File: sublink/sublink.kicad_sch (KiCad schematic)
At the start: 27 parts

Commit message: wip schematic probably done
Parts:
- removed BT?: L402036, symbol Device:Battery
- removed C?: 100n, symbol Device:C
- removed D? (x15): LED, symbol Device:LED
- removed Q? (x4): Q_NMOS_DGS, symbol Device:Q_NMOS_DGS
- removed Q?: Q_PMOS_DGS, symbol Device:Q_PMOS_DGS
- removed R?: 330, symbol Device:R
- removed R?: 2k7, symbol Device:R
- removed U?: ATtiny414-SS, Package_SO:SOIC-14_3.9x8.7mm_P1.27mm, symbol MCU_Microchip_ATtiny:ATtiny414-SS
- removed U?: 4001, symbol 4xxx:4001
- removed U?: AP9101CK, Package_TO_SOT_SMD:SOT-23-5, symbol Battery_Management:AP9101CK
- added BT1: 3V7, Connector_PinHeader_2.54mm:PinHeader_1x02_P2.54mm_Vertical, symbol Device:Battery
- added D1, D2, D3: LED, LED_SMD:LED_0805_2012Metric_Pad1.15x1.40mm_HandSolder, symbol Device:LED
- added D10, D11, D12, D13, D14, D15, D16, D17, D18, D19, D20, D21, D4, D5, D6, D7, D8, D9: LED_Small, LED_SMD:LED_0805_2012Metric_Pad1.15x1.40mm_HandSolder, symbol Device:LED_Small
- added D22: DNP, Diode_SMD:D_SOD-323_HandSoldering, symbol Device:D_Small
- added D23: BAS21HT1G, Diode_SMD:D_SOD-323_HandSoldering, symbol Device:D_Small
- added J1: Conn_01x03_Female, Connector_PinHeader_2.54mm:PinHeader_1x03_P2.54mm_Horizontal, symbol Connector:Conn_01x03_Female
- added Q1: YJL2305A, Package_TO_SOT_SMD:SOT-23, symbol Device:Q_PMOS_DGS
- added R1, R2, R3, R4, R5, R6, R7, R8: R_Small, Resistor_SMD:R_0805_2012Metric_Pad1.20x1.40mm_HandSolder, symbol Device:R_Small
- added R9: 10k, Resistor_SMD:R_0805_2012Metric_Pad1.20x1.40mm_HandSolder, symbol Device:R_Small
- added SW1, SW2, SW3: SW_Push, Button_Switch_SMD:SW_SPST_Omron_B3FS-100xP, symbol Switch:SW_Push
- added U1: ATtiny414-SS, Package_SO:SOIC-14_3.9x8.7mm_P1.27mm, symbol MCU_Microchip_ATtiny:ATtiny414-SS
- added U2: OKY3402, sublink_custom:OKY3402, symbol custom_sublink:OKY3402
- added U3: JS202011, sublink_custom:JS202011, symbol custom_sublink:JS202011
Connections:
- net GND: now also BT1.2 (-), D1.1 (K), D2.1 (K), D3.1 (K), J1.1 (Pin_1), R9.1, SW1.1, SW2.1, SW3.1, U1.14 (GND), U2.1 (USB-), U2.3 (B-)
- net UPDI: now also J1.2 (Pin_2), U1.10 (~{RESET}/PA0)
- new net: D23.2 (A), Q1.2 (G), R9.2, U2.2 (USB+)
- new net: BT1.1 (+), D22.2 (A), Q1.1 (D), U2.4 (B+)
- new net: R4.2, U1.13 (PA3)
- new net: J1.3 (Pin_3), U3.3
- new net: D2.2 (A), R2.2
- new net: R6.2, U1.3 (PA5)
- new net: R2.1, U1.8 (PB1)
- new net: R1.1, U1.9 (PB0)
- new net: D1.2 (A), R1.2
- new net: R7.2, U1.4 (PA6)
- new net: D3.2 (A), R3.2
- new net: D22.1 (K), D23.1 (K), Q1.3 (S), U3.1
- new net: R3.1, U1.7 (PB2)
- new net: R5.2, U1.2 (PA4)
- new net: R8.2, U1.5 (PA7)
- new net L0: D4.2 (A), D5.1 (K), D6.1 (K), D7.2 (A), D8.1 (K), D9.2 (A), R4.1
- new net L1: D10.1 (K), D11.2 (A), D12.1 (K), D13.2 (A), D20.1 (K), D21.2 (A), D6.2 (A), D7.1 (K), R5.1
- new net L2: D10.2 (A), D11.1 (K), D14.1 (K), D15.2 (A), D18.1 (K), D19.2 (A), D8.2 (A), D9.1 (K), R6.1
- new net L3: D12.2 (A), D13.1 (K), D14.2 (A), D15.1 (K), D16.1 (K), D17.2 (A), D4.1 (K), D5.2 (A), R7.1
- new net L4: D16.2 (A), D17.1 (K), D18.2 (A), D19.1 (K), D20.2 (A), D21.1 (K), R8.1
- new net VCC: U1.1 (VCC), U3.5
- new net butt1: SW1.2, U1.6 (PB3)
- new net butt2: SW2.2, U1.11 (PA1)
- new net butt3: SW3.2, U1.12 (PA2)
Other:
- note added: "Pullups internal"

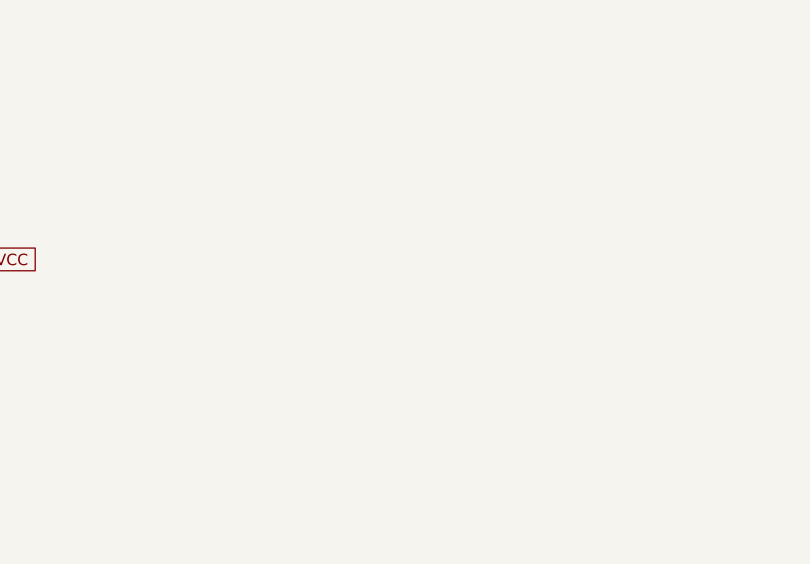
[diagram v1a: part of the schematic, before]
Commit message: wip board outline, led placement
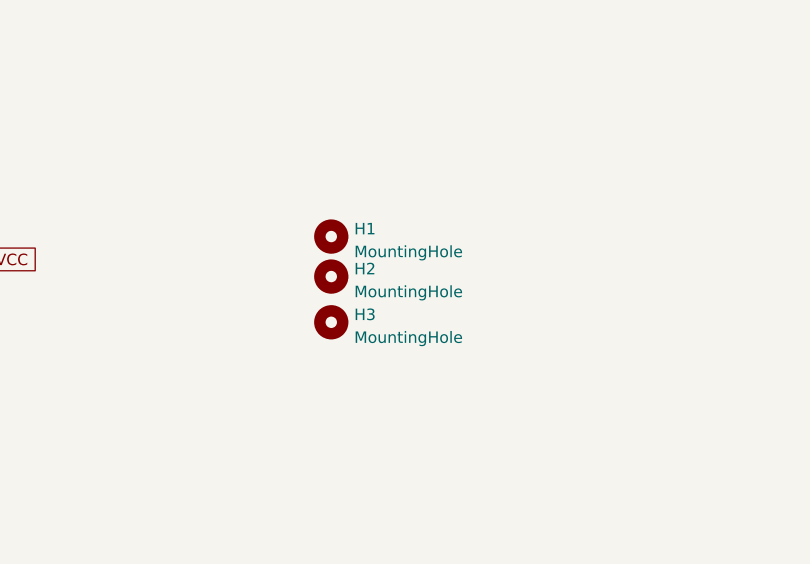
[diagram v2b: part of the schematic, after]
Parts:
- added H1, H2, H3: MountingHole, MountingHole:MountingHole_2.2mm_M2, symbol Mechanical:MountingHole
- J1: footprint Connector_PinHeader_2.54mm:PinHeader_1x03_P2.54mm_Horizontal -> Connector_PinSocket_2.54mm:PinSocket_1x03_P2.54mm_Horizontal
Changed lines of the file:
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@@
     (property "Reference" "J1" (id 0) (at 108.585 108.585 0))
     (property "Value" "Conn_01x03_Female" (id 1) (at 108.585 111.125 0))
-    (property "Footprint" "Connector_PinHeader_2.54mm:PinHeader_1x03_P2.54mm_Horizontal" (id 2) (at 108.585 118.11 0)
+    (property "Footprint" "Connector_PinSocket_2.54mm:PinSocket_1x03_P2.54mm_Horizontal" (id 2) (at 108.585 118.11 0)
       (effects (font (size 1.27 1.27)) hide)
     )
@@
     (pin "1")
     (pin "2")
+  )
+  (symbol (lib_id "Mechanical:MountingHole") (at 183.515 103.505 0) (unit 1)
+    (in_bom yes) (on_board yes) (fields_autoplaced)
+    (property "Reference" "H3" (id 0) (at 186.055 102.6703 0)
+      (effects (font (size 1.27 1.27)) (justify left))
+    )
+    (property "Value" "MountingHole" (id 1) (at 186.055 105.2072 0)
+      (effects (font (size 1.27 1.27)) (justify left))
+    )
+    (property "Footprint" "MountingHole:MountingHole_2.2mm_M2" (id 2) (at 183.515 103.505 0)
+      (effects (font (size 1.27 1.27)) hide)
+    )
+    (property "Datasheet" "~" (id 3) (at 183.515 103.505 0)
+      (effects (font (size 1.27 1.27)) hide)
+    )
   )
   (symbol (lib_id "Device:R_Small") (at 86.36 50.8 0) (unit 1)
@@
     (pin "1")
     (pin "2")
+  )
+  (symbol (lib_id "Mechanical:MountingHole") (at 183.515 98.425 0) (unit 1)
+    (in_bom yes) (on_board yes) (fields_autoplaced)
+    (property "Reference" "H2" (id 0) (at 186.055 97.5903 0)
+      (effects (font (size 1.27 1.27)) (justify left))
+    )
+    (property "Value" "MountingHole" (id 1) (at 186.055 100.1272 0)
+      (effects (font (size 1.27 1.27)) (justify left))
+    )
+    (property "Footprint" "MountingHole:MountingHole_2.2mm_M2" (id 2) (at 183.515 98.425 0)
+      (effects (font (size 1.27 1.27)) hide)
+    )
+    (property "Datasheet" "~" (id 3) (at 183.515 98.425 0)
+      (effects (font (size 1.27 1.27)) hide)
+    )
   )
   (symbol (lib_id "Device:LED_Small") (at 196.85 57.15 180) (unit 1)
@@
     (pin "2")
   )
+  (symbol (lib_id "Mechanical:MountingHole") (at 183.515 93.98 0) (unit 1)
+    (in_bom yes) (on_board yes) (fields_autoplaced)
+    (property "Reference" "H1" (id 0) (at 186.055 93.1453 0)
+      (effects (font (size 1.27 1.27)) (justify left))
+    )
+    (property "Value" "MountingHole" (id 1) (at 186.055 95.6822 0)
+      (effects (font (size 1.27 1.27)) (justify left))
+    )
+    (property "Footprint" "MountingHole:MountingHole_2.2mm_M2" (id 2) (at 183.515 93.98 0)
+      (effects (font (size 1.27 1.27)) hide)
+    )
+    (property "Datasheet" "~" (id 3) (at 183.515 93.98 0)
+      (effects (font (size 1.27 1.27)) hide)
+    )
+  )
   (sheet_instances
     (path "/" (page "1"))
@@
       (reference "D23") (unit 1) (value "BAS21HT1G") (footprint "Diode_SMD:D_SOD-323_HandSoldering")
     )
+    (path "/fc4eec4b-8584-44a9-b4ee-f38c1daffec1"
+      (reference "H1") (unit 1) (value "MountingHole") (footprint "MountingHole:MountingHole_2.2mm_M2")
+    )
+    (path "/e7677e64-5f73-401f-9091-20b35805b2ae"
+      (reference "H2") (unit 1) (value "MountingHole") (footprint "MountingHole:MountingHole_2.2mm_M2")
+    )
+    (path "/3b424eec-cabe-480a-a474-53116b544129"
+      (reference "H3") (unit 1) (value "MountingHole") (footprint "MountingHole:MountingHole_2.2mm_M2")
+    )
     (path "/170ef5e5-14d8-49d3-8e99-cca39c60c343"
-      (reference "J1") (unit 1) (value "Conn_01x03_Female") (footprint "Connector_PinHeader_2.54mm:PinHeader_1x03_P2.54mm_Horizontal")
+      (reference "J1") (unit 1) (value "Conn_01x03_Female") (footprint "Connector_PinSocket_2.54mm:PinSocket_1x03_P2.54mm_Horizontal")
     )
     (path "/aa0a099c-479d-4909-8f65-0af88e650102"

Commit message: wip bottom side component positioning
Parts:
- removed J1: Conn_01x03_Female, Connector_PinSocket_2.54mm:PinSocket_1x03_P2.54mm_Horizontal, symbol Connector:Conn_01x03_Female
- added J1: ZL315-4SGH, Connector_Harwin:Harwin_M20-89004xx_1x04_P2.54mm_Horizontal, symbol Connector:Conn_01x04_Female
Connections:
- net GND: now also J1.3 (Pin_3)
- net UPDI: now also J1.2 (Pin_2)
- net at U3.3: now also J1.1 (Pin_1)
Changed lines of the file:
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@@
-    (stroke (width 0) (type default) (color 0 0 0 0))
-  )
-  (wire (pts (xy 118.11 120.65) (xy 113.665 120.65))
     (stroke (width 0) (type default) (color 0 0 0 0))
   )
@@
     (stroke (width 0) (type default) (color 0 0 0 0))
   )
+  (wire (pts (xy 111.76 120.65) (xy 118.11 120.65))
+    (stroke (width 0) (type default) (color 0 0 0 0))
+  )
   (wire (pts (xy 96.52 74.93) (xy 127 74.93))
     (stroke (width 0) (type default) (color 0 0 0 0))
@@
     (stroke (width 0) (type default) (color 0 0 0 0))
   )
+  (wire (pts (xy 111.76 118.11) (xy 120.015 118.11))
+    (stroke (width 0) (type default) (color 0 0 0 0))
+  )
   (wire (pts (xy 62.865 107.315) (xy 62.865 114.935))
     (stroke (width 0) (type default) (color 0 0 0 0))
@@
     (stroke (width 0) (type default) (color 0 0 0 0))
   )
-  (wire (pts (xy 113.665 115.57) (xy 120.015 115.57))
+  (wire (pts (xy 111.76 115.57) (xy 120.015 115.57))
     (stroke (width 0) (type default) (color 0 0 0 0))
   )
@@
   )
   (wire (pts (xy 214.63 39.37) (xy 217.17 39.37))
-    (stroke (width 0) (type default) (color 0 0 0 0))
-  )
-  (wire (pts (xy 113.665 118.11) (xy 120.015 118.11))
     (stroke (width 0) (type default) (color 0 0 0 0))
   )
@@
     (pin "1")
     (pin "2")
-  )
-  (symbol (lib_id "Connector:Conn_01x03_Female") (at 108.585 118.11 180) (unit 1)
-    (in_bom yes) (on_board yes)
-    (property "Reference" "J1" (id 0) (at 108.585 108.585 0))
-    (property "Value" "Conn_01x03_Female" (id 1) (at 108.585 111.125 0))
-    (property "Footprint" "Connector_PinSocket_2.54mm:PinSocket_1x03_P2.54mm_Horizontal" (id 2) (at 108.585 118.11 0)
-      (effects (font (size 1.27 1.27)) hide)
-    )
-    (property "Datasheet" "~" (id 3) (at 108.585 118.11 0)
-      (effects (font (size 1.27 1.27)) hide)
-    )
-    (pin "1")
-    (pin "2")
-    (pin "3")
   )
   (symbol (lib_id "Device:LED_Small") (at 201.93 41.91 180) (unit 1)
@@
       (effects (font (size 1.27 1.27)) hide)
     )
+  )
+  (symbol (lib_id "Connector:Conn_01x04_Female") (at 106.68 118.11 0) (mirror y) (unit 1)
+    (in_bom yes) (on_board yes) (fields_autoplaced)
+    (property "Reference" "J1" (id 0) (at 107.315 110.49 0))
+    (property "Value" "ZL315-4SGH" (id 1) (at 107.315 113.03 0))
+    (property "Footprint" "Connector_Harwin:Harwin_M20-89004xx_1x04_P2.54mm_Horizontal" (id 2) (at 106.68 118.11 0)
+      (effects (font (size 1.27 1.27)) hide)
+    )
+    (property "Datasheet" "~" (id 3) (at 106.68 118.11 0)
+      (effects (font (size 1.27 1.27)) hide)
+    )
+    (pin "1")
+    (pin "2")
+    (pin "3")
+    (pin "4")
   )
   (symbol (lib_id "Device:LED_Small") (at 196.85 57.15 180) (unit 1)
@@
       (reference "H3") (unit 1) (value "MountingHole") (footprint "MountingHole:MountingHole_2.2mm_M2")
     )
-    (path "/170ef5e5-14d8-49d3-8e99-cca39c60c343"
-      (reference "J1") (unit 1) (value "Conn_01x03_Female") (footprint "Connector_PinSocket_2.54mm:PinSocket_1x03_P2.54mm_Horizontal")
+    (path "/e87aa614-7589-49fe-ae6e-b8c6a9ab4dff"
+      (reference "J1") (unit 1) (value "ZL315-4SGH") (footprint "Connector_Harwin:Harwin_M20-89004xx_1x04_P2.54mm_Horizontal")
     )
     (path "/aa0a099c-479d-4909-8f65-0af88e650102"
